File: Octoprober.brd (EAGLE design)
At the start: 130.8 x 86.9 mm, 111 parts, among them J1 10118193-0001LF, J2 26-60-4020, P1 TC33X-1, SW1 101-0134-EV, SW2 EVQ-Q2203W, SW3 EVQ-Q2203W, SW4 EVQ-Q2203W, SW5 EVQ-Q2203W, U1 P8X32A-M44, U10 MAX31855KASA+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

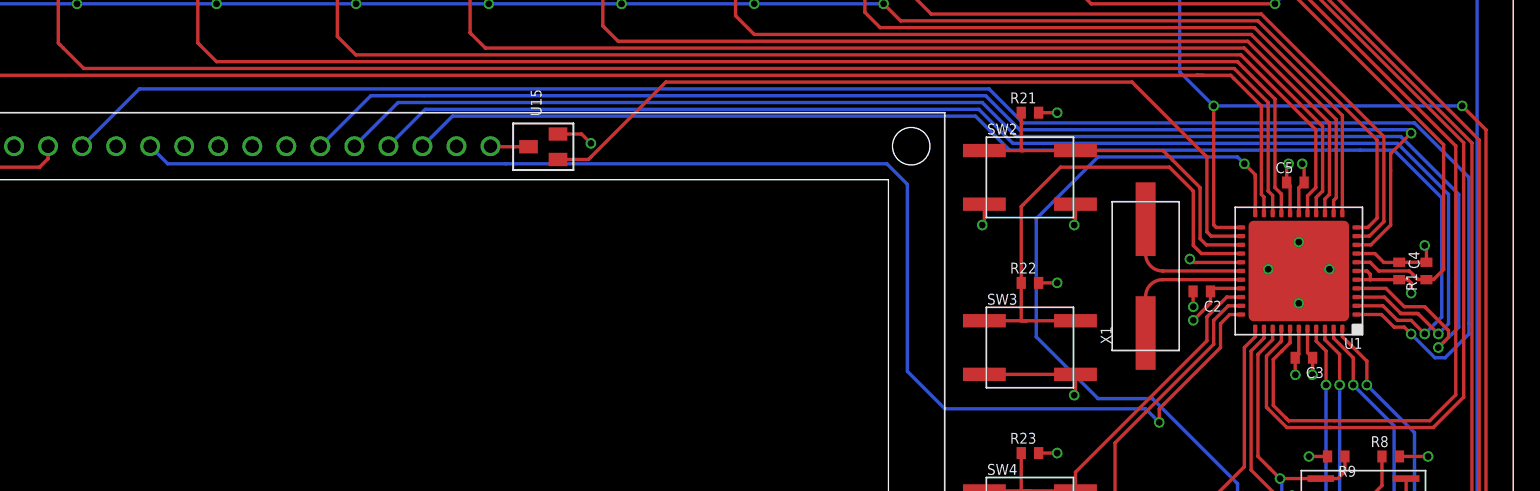
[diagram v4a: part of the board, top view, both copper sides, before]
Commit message: Rerouted I/O for LCD around mounting hole
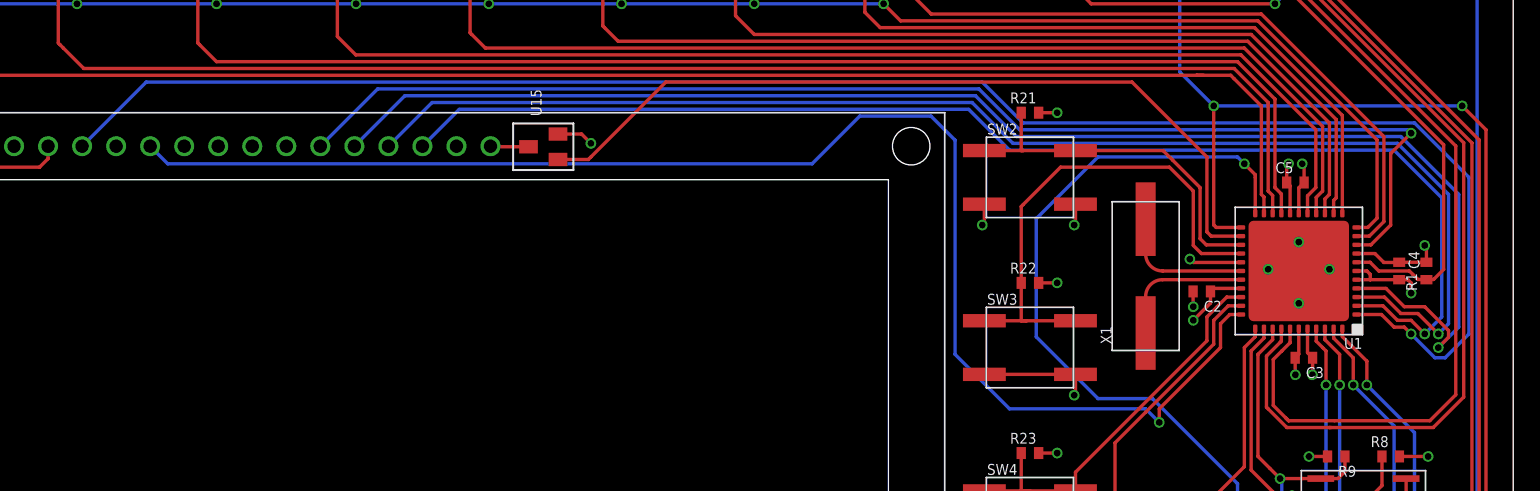
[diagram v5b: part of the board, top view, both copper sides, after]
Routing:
- net LCD_E: track 103.1 -> 107.2 mm
- net LCD_D6: track 102.1 -> 101.3 mm
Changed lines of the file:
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@@
 <wire x1="119.108" y1="47.169" x2="120.979" y2="47.169" width="0.254" layer="1"/>
 <wire x1="120.979" y1="47.169" x2="121.92" y2="46.228" width="0.254" layer="1"/>
-<wire x1="24.002" y1="59.73" x2="28.28" y2="64.008" width="0.254" layer="16"/>
-<wire x1="28.28" y1="64.008" x2="91.694" y2="64.008" width="0.254" layer="16"/>
-<wire x1="91.694" y1="64.008" x2="94.234" y2="61.468" width="0.254" layer="16"/>
 <wire x1="94.234" y1="61.468" x2="123.444" y2="61.468" width="0.254" layer="16"/>
 <wire x1="123.444" y1="61.468" x2="127.508" y2="57.404" width="0.254" layer="16"/>
-<wire x1="127.508" y1="57.404" x2="127.508" y2="46.482" width="0.254" layer="16"/>
+<wire x1="127.508" y1="57.404" x2="127.508" y2="45.72" width="0.254" layer="16"/>
 <via x="123.19" y="45.72" extent="1-16" drill="0.5"/>
 <wire x1="123.19" y1="45.72" x2="122.682" y2="46.228" width="0.254" layer="1"/>
 <wire x1="122.682" y1="46.228" x2="121.92" y2="46.228" width="0.254" layer="1"/>
-<wire x1="127.508" y1="46.482" x2="127.508" y2="45.72" width="0.254" layer="16"/>
 <wire x1="127.508" y1="45.72" x2="125.73" y2="43.942" width="0.254" layer="16"/>
 <wire x1="125.73" y1="43.942" x2="124.968" y2="43.942" width="0.254" layer="16"/>
 <wire x1="124.968" y1="43.942" x2="123.19" y2="45.72" width="0.254" layer="16"/>
+<wire x1="24.002" y1="59.73" x2="28.788" y2="64.516" width="0.254" layer="16"/>
+<wire x1="28.788" y1="64.516" x2="91.186" y2="64.516" width="0.254" layer="16"/>
+<wire x1="91.186" y1="64.516" x2="94.234" y2="61.468" width="0.254" layer="16"/>
 </signal>
 <signal name="3.3V">
@@
 <wire x1="109.653" y1="47.169" x2="108.966" y2="46.482" width="0.254" layer="1"/>
 <wire x1="108.966" y1="46.482" x2="108.966" y2="44.704" width="0.254" layer="1"/>
-<wire x1="108.966" y1="44.704" x2="104.775" y2="40.513" width="0.254" layer="1"/>
+<wire x1="108.966" y1="44.704" x2="104.394" y2="40.132" width="0.254" layer="1"/>
 <wire x1="29.082" y1="59.73" x2="30.392" y2="58.42" width="0.254" layer="16"/>
-<wire x1="30.392" y1="58.42" x2="55.626" y2="58.42" width="0.254" layer="16"/>
-<wire x1="55.626" y1="58.42" x2="84.06345625" y2="58.42" width="0.254" layer="16"/>
-<wire x1="84.06345625" y1="58.42" x2="85.598" y2="56.88545625" width="0.254" layer="16"/>
-<wire x1="85.598" y1="56.88545625" x2="85.598" y2="42.926" width="0.254" layer="16"/>
-<wire x1="85.598" y1="42.926" x2="88.392" y2="40.132" width="0.254" layer="16"/>
-<wire x1="88.392" y1="40.132" x2="103.378" y2="40.132" width="0.254" layer="16"/>
+<wire x1="93.218" y1="40.132" x2="103.378" y2="40.132" width="0.254" layer="16"/>
 <wire x1="103.378" y1="40.132" x2="104.394" y2="39.116" width="0.254" layer="16"/>
 <via x="104.394" y="39.116" extent="1-16" drill="0.5"/>
 <wire x1="104.394" y1="39.116" x2="104.394" y2="40.132" width="0.254" layer="1"/>
-<wire x1="104.394" y1="40.132" x2="104.775" y2="40.513" width="0.254" layer="1"/>
+<wire x1="30.392" y1="58.42" x2="78.486" y2="58.42" width="0.254" layer="16"/>
+<wire x1="78.486" y1="58.42" x2="82.042" y2="61.976" width="0.254" layer="16"/>
+<wire x1="82.042" y1="61.976" x2="87.35795" y2="61.976" width="0.254" layer="16"/>
+<wire x1="87.35795" y1="61.976" x2="89.154" y2="60.17995" width="0.254" layer="16"/>
+<wire x1="89.154" y1="60.17995" x2="89.154" y2="44.196" width="0.254" layer="16"/>
+<wire x1="89.154" y1="44.196" x2="93.218" y2="40.132" width="0.254" layer="16"/>
 </signal>
 <signal name="LCD_D7">
@@
 <wire x1="121.091" y1="47.819" x2="122.174" y2="46.736" width="0.254" layer="1"/>
 <wire x1="122.174" y1="46.736" x2="123.19" y2="46.736" width="0.254" layer="1"/>
-<wire x1="49.402" y1="59.73" x2="51.648" y2="61.976" width="0.254" layer="16"/>
-<wire x1="51.648" y1="61.976" x2="90.678" y2="61.976" width="0.254" layer="16"/>
-<wire x1="90.678" y1="61.976" x2="93.218" y2="59.436" width="0.254" layer="16"/>
-<wire x1="93.218" y1="59.436" x2="119.38" y2="59.436" width="0.254" layer="16"/>
-<wire x1="119.38" y1="59.436" x2="121.92" y2="59.436" width="0.254" layer="16"/>
+<wire x1="49.402" y1="59.73" x2="52.156" y2="62.484" width="0.254" layer="16"/>
+<wire x1="90.17" y1="62.484" x2="93.218" y2="59.436" width="0.254" layer="16"/>
+<wire x1="93.218" y1="59.436" x2="121.92" y2="59.436" width="0.254" layer="16"/>
 <wire x1="121.92" y1="59.436" x2="125.476" y2="55.88" width="0.254" layer="16"/>
 <wire x1="125.476" y1="55.88" x2="125.476" y2="46.99" width="0.254" layer="16"/>
@@
 <via x="124.206" y="45.72" extent="1-16" drill="0.5"/>
 <wire x1="124.206" y1="45.72" x2="123.19" y2="46.736" width="0.254" layer="1"/>
+<wire x1="52.156" y1="62.484" x2="90.17" y2="62.484" width="0.254" layer="16"/>
 </signal>
 <signal name="LCD_D6">
@@
 <wire x1="119.108" y1="48.469" x2="121.203" y2="48.469" width="0.254" layer="1"/>
 <wire x1="121.203" y1="48.469" x2="122.428" y2="47.244" width="0.254" layer="1"/>
-<wire x1="122.428" y1="47.244" x2="123.698" y2="47.244" width="0.254" layer="1"/>
-<wire x1="46.862" y1="59.73" x2="49.616" y2="62.484" width="0.254" layer="16"/>
-<wire x1="49.616" y1="62.484" x2="90.932" y2="62.484" width="0.254" layer="16"/>
-<wire x1="90.932" y1="62.484" x2="93.472" y2="59.944" width="0.254" layer="16"/>
+<wire x1="46.862" y1="59.73" x2="50.124" y2="62.992" width="0.254" layer="16"/>
+<wire x1="90.424" y1="62.992" x2="93.472" y2="59.944" width="0.254" layer="16"/>
 <wire x1="93.472" y1="59.944" x2="122.174" y2="59.944" width="0.254" layer="16"/>
 <wire x1="122.174" y1="59.944" x2="125.984" y2="56.134" width="0.254" layer="16"/>
@@
 <wire x1="125.222" y1="45.72" x2="123.698" y2="47.244" width="0.254" layer="1"/>
 <wire x1="123.698" y1="47.244" x2="122.428" y2="47.244" width="0.254" layer="1"/>
+<wire x1="50.124" y1="62.992" x2="90.424" y2="62.992" width="0.254" layer="16"/>
 </signal>
 <signal name="LCD_D5">
@@
 <wire x1="121.315" y1="49.119" x2="122.682" y2="47.752" width="0.254" layer="1"/>
 <wire x1="122.682" y1="47.752" x2="124.206" y2="47.752" width="0.254" layer="1"/>
-<wire x1="44.322" y1="59.73" x2="47.584" y2="62.992" width="0.254" layer="16"/>
-<wire x1="47.584" y1="62.992" x2="91.186" y2="62.992" width="0.254" layer="16"/>
-<wire x1="91.186" y1="62.992" x2="93.726" y2="60.452" width="0.254" layer="16"/>
+<wire x1="44.322" y1="59.73" x2="48.092" y2="63.5" width="0.254" layer="16"/>
+<wire x1="90.678" y1="63.5" x2="93.726" y2="60.452" width="0.254" layer="16"/>
 <wire x1="93.726" y1="60.452" x2="122.428" y2="60.452" width="0.254" layer="16"/>
 <wire x1="122.428" y1="60.452" x2="126.746" y2="56.134" width="0.254" layer="16"/>
 <wire x1="126.746" y1="56.134" x2="126.746" y2="46.228" width="0.254" layer="16"/>
-<wire x1="126.746" y1="46.228" x2="126.238" y2="45.72" width="0.254" layer="16"/>
-<wire x1="126.238" y1="45.72" x2="125.222" y2="44.704" width="0.254" layer="16"/>
+<wire x1="126.746" y1="46.228" x2="125.222" y2="44.704" width="0.254" layer="16"/>
 <via x="125.222" y="44.704" extent="1-16" drill="0.5"/>
 <wire x1="125.222" y1="44.704" x2="125.984" y2="45.466" width="0.254" layer="1"/>
 <wire x1="125.984" y1="45.466" x2="125.984" y2="45.974" width="0.254" layer="1"/>
 <wire x1="125.984" y1="45.974" x2="124.206" y2="47.752" width="0.254" layer="1"/>
+<wire x1="48.092" y1="63.5" x2="90.678" y2="63.5" width="0.254" layer="16"/>
 </signal>
 <signal name="LCD_D4">
@@
 <wire x1="119.108" y1="52.369" x2="120.187" y2="52.369" width="0.254" layer="1"/>
 <wire x1="120.187" y1="52.369" x2="121.666" y2="53.848" width="0.254" layer="1"/>
-<wire x1="121.666" y1="53.848" x2="121.666" y2="57.912" width="0.254" layer="1"/>
-<wire x1="41.782" y1="59.73" x2="45.552" y2="63.5" width="0.254" layer="16"/>
-<wire x1="45.552" y1="63.5" x2="49.53" y2="63.5" width="0.254" layer="16"/>
-<wire x1="49.53" y1="63.5" x2="91.44" y2="63.5" width="0.254" layer="16"/>
-<wire x1="91.44" y1="63.5" x2="93.98" y2="60.96" width="0.254" layer="16"/>
+<wire x1="121.666" y1="53.848" x2="121.666" y2="59.182" width="0.254" layer="1"/>
+<wire x1="41.782" y1="59.73" x2="46.06" y2="64.008" width="0.254" layer="16"/>
+<wire x1="90.932" y1="64.008" x2="93.98" y2="60.96" width="0.254" layer="16"/>
 <wire x1="93.98" y1="60.96" x2="122.936" y2="60.96" width="0.254" layer="16"/>
 <wire x1="122.936" y1="60.96" x2="123.19" y2="60.706" width="0.254" layer="16"/>
 <via x="123.19" y="60.706" extent="1-16" drill="0.5"/>
 <wire x1="123.19" y1="60.706" x2="121.666" y2="59.182" width="0.254" layer="1"/>
-<wire x1="121.666" y1="59.182" x2="121.666" y2="57.912" width="0.254" layer="1"/>
+<wire x1="46.06" y1="64.008" x2="90.932" y2="64.008" width="0.254" layer="16"/>
 </signal>
 <signal name="TP_T+_0">

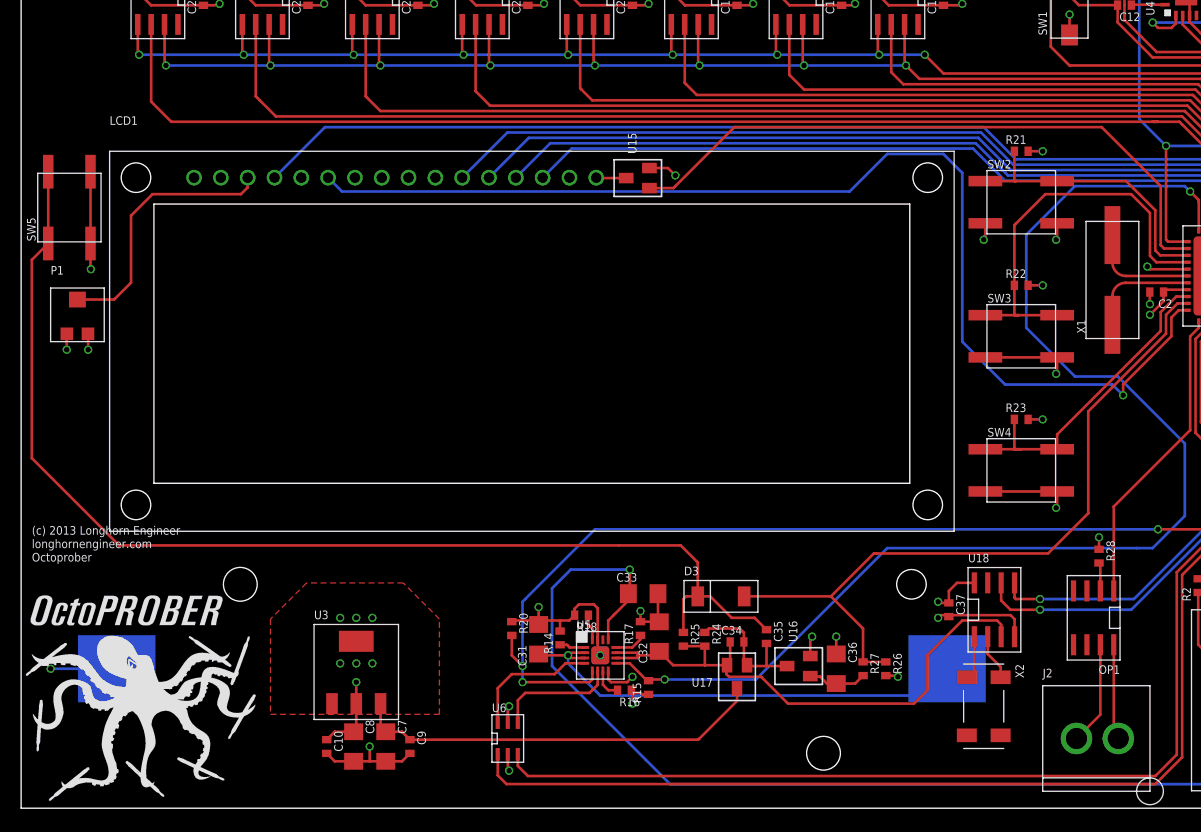
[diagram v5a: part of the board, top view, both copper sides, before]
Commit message: Working on Silkscreen
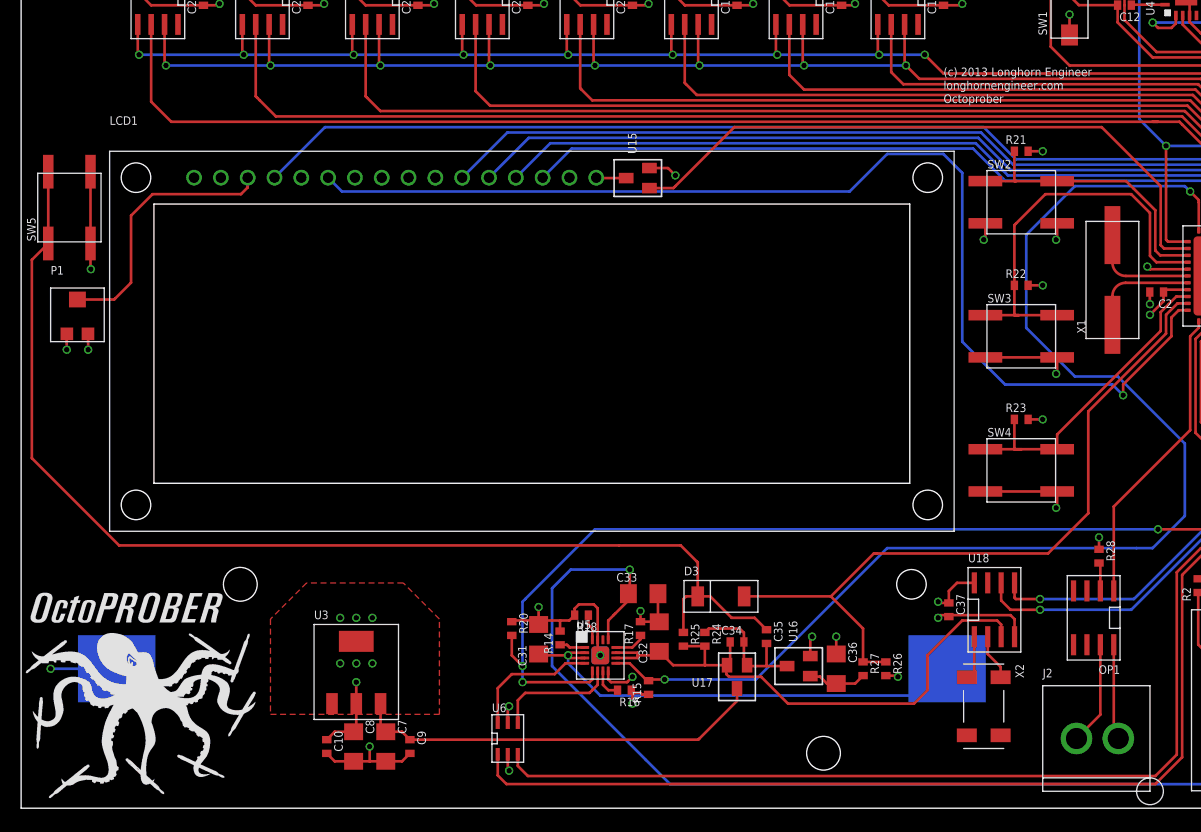
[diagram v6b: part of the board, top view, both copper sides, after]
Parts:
- moved U$1 96.7 mm to (87.4, 64.3)
- moved U$2 0.25 mm to (-0.51, 0.76)
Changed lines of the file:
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@@
 <element name="C13" library="PP_Passives" package="0402" value="0.1uF" x="110.363" y="82.804" rot="R90"/>
 <element name="C14" library="PP_Passives" package="0402" value="0.1uF" x="124.333" y="78.486" rot="R90"/>
-<element name="U$1" library="PP_Aesthetics" package="LHE_FRAME" value="LHE_FRAME" x="1.016" y="20.828">
-<attribute name="REVNUM" value="REV 0" x="67.056" y="-66.802" size="1.778" layer="27" display="off"/>
-<attribute name="DNAME" value="Parker Dillmann" x="67.056" y="-66.802" size="1.778" layer="27" display="off"/>
+<element name="U$1" library="PP_Aesthetics" package="LHE_FRAME" value="LHE_FRAME" x="87.376" y="64.262">
+<attribute name="REVNUM" value="REV 0" x="153.416" y="-23.368" size="1.778" layer="27" display="off"/>
+<attribute name="DNAME" value="Parker Dillmann" x="153.416" y="-23.368" size="1.778" layer="27" display="off"/>
 </element>
 <element name="LCD1" library="PP_Displays" package="CHAR_DISPLAY_1602_COUNTERSINK" value="" x="8.382" y="62.23"/>
@@
 <element name="R26" library="PP_Passives" package="0402" value="100K" x="81.915" y="13.208" rot="R270"/>
 <element name="R27" library="PP_Passives" package="0402" value="300K" x="79.756" y="13.208" rot="R270"/>
-<element name="U$2" library="PP_Aesthetics" package="OCTOPROBER_LOGO" value="OCTOPROBER_LOGONORMAL" x="-0.508" y="0.508"/>
+<element name="U$2" library="PP_Aesthetics" package="OCTOPROBER_LOGO" value="OCTOPROBER_LOGONORMAL" x="-0.508" y="0.762"/>
 <element name="J2" library="PP_Connectors" package="MOLEX_KK_2" value="26-60-4020" x="101.854" y="6.604"/>
 <element name="OP1" library="PP_DigitalIC" package="SOIC-8" value="" x="101.6" y="18.034" rot="R180"/>

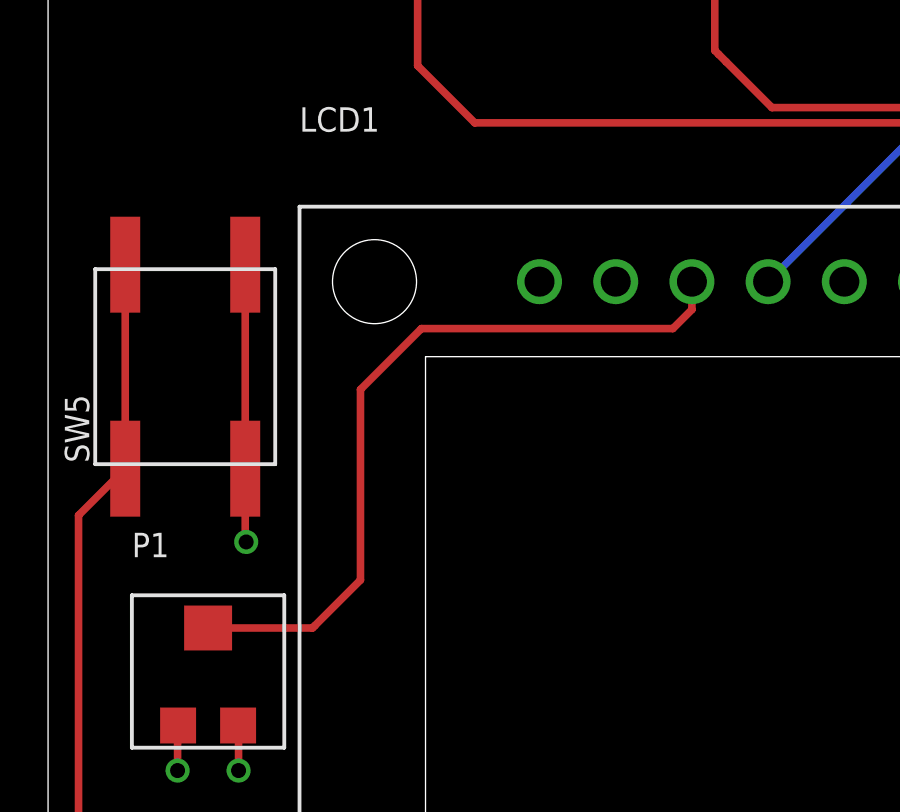
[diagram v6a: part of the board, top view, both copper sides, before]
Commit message: Fixed some traces. Looking good. Silkscreen next.
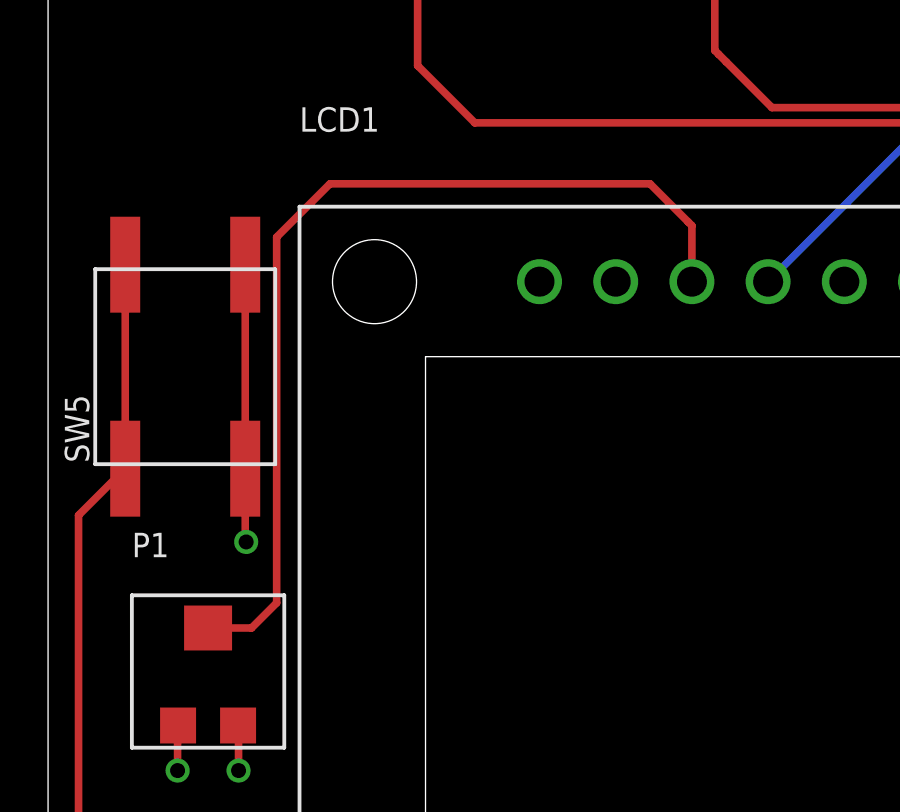
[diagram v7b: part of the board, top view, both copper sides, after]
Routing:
- net CONTRAST: track 25.2 -> 31.8 mm
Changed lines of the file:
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@@
 <?xml version="1.0" encoding="utf-8"?>
 <!DOCTYPE eagle SYSTEM "eagle.dtd">
-<eagle version="6.5.0">
+<eagle version="6.3">
 <drawing>
 <settings>
@@
 <wire x1="115.57" y1="82.144" x2="115.57" y2="80.518" width="0.254" layer="1"/>
 <wire x1="6.572" y1="60.296" x2="6.572" y2="53.496" width="0.254" layer="1"/>
-<wire x1="6.604" y1="37.846" x2="6.604" y2="38.1" width="0.254" layer="2"/>
 <wire x1="6.572" y1="53.496" x2="6.572" y2="51.086" width="0.254" layer="1"/>
 <wire x1="6.572" y1="51.086" x2="6.604" y2="51.054" width="0.254" layer="1"/>
@@
 <contactref element="LCD1" pad="3"/>
 <contactref element="P1" pad="2"/>
-<wire x1="21.462" y1="59.73" x2="21.462" y2="58.8" width="0.254" layer="1"/>
-<wire x1="21.462" y1="58.8" x2="20.828" y2="58.166" width="0.254" layer="1"/>
-<wire x1="20.828" y1="58.166" x2="12.446" y2="58.166" width="0.254" layer="1"/>
-<wire x1="12.446" y1="58.166" x2="10.414" y2="56.134" width="0.254" layer="1"/>
-<wire x1="10.414" y1="56.134" x2="10.414" y2="49.784" width="0.254" layer="1"/>
-<wire x1="10.414" y1="49.784" x2="8.89" y2="48.26" width="0.254" layer="1"/>
-<wire x1="8.89" y1="48.26" x2="8.816" y2="48.186" width="0.254" layer="1"/>
-<wire x1="8.816" y1="48.186" x2="5.334" y2="48.186" width="0.254" layer="1"/>
+<wire x1="5.334" y1="48.186" x2="6.784" y2="48.186" width="0.254" layer="1"/>
+<wire x1="6.784" y1="48.186" x2="7.62" y2="49.022" width="0.254" layer="1"/>
+<wire x1="7.62" y1="49.022" x2="7.62" y2="61.214" width="0.254" layer="1"/>
+<wire x1="7.62" y1="61.214" x2="9.398" y2="62.992" width="0.254" layer="1"/>
+<wire x1="9.398" y1="62.992" x2="20.066" y2="62.992" width="0.254" layer="1"/>
+<wire x1="20.066" y1="62.992" x2="21.336" y2="61.722" width="0.254" layer="1"/>
+<wire x1="21.336" y1="61.722" x2="21.462" y2="61.596" width="0.254" layer="1"/>
+<wire x1="21.462" y1="61.596" x2="21.462" y2="59.73" width="0.254" layer="1"/>
 </signal>
 <signal name="BK_GND">
@@
 </signal>
 </signals>
-<errors>
-</errors>
 </board>
 </drawing>
